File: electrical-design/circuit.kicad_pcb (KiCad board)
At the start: 4 copper layers, 100 x 70 mm, 42 parts, among them J1 AVR-ISP-10, J2 Conn_01x03_Female, J3 Conn_01x03_Female, Q1 2N3906, Q2 2N3906, Q3 2N3906, Q4 2N3906, SW1 SW_Push, SW2 SW_DIP_x04, SW3 SW_Push, U1 ATmega8A-P, U2 LTC-4627JD, U3 NE555P, Y1 16MHz

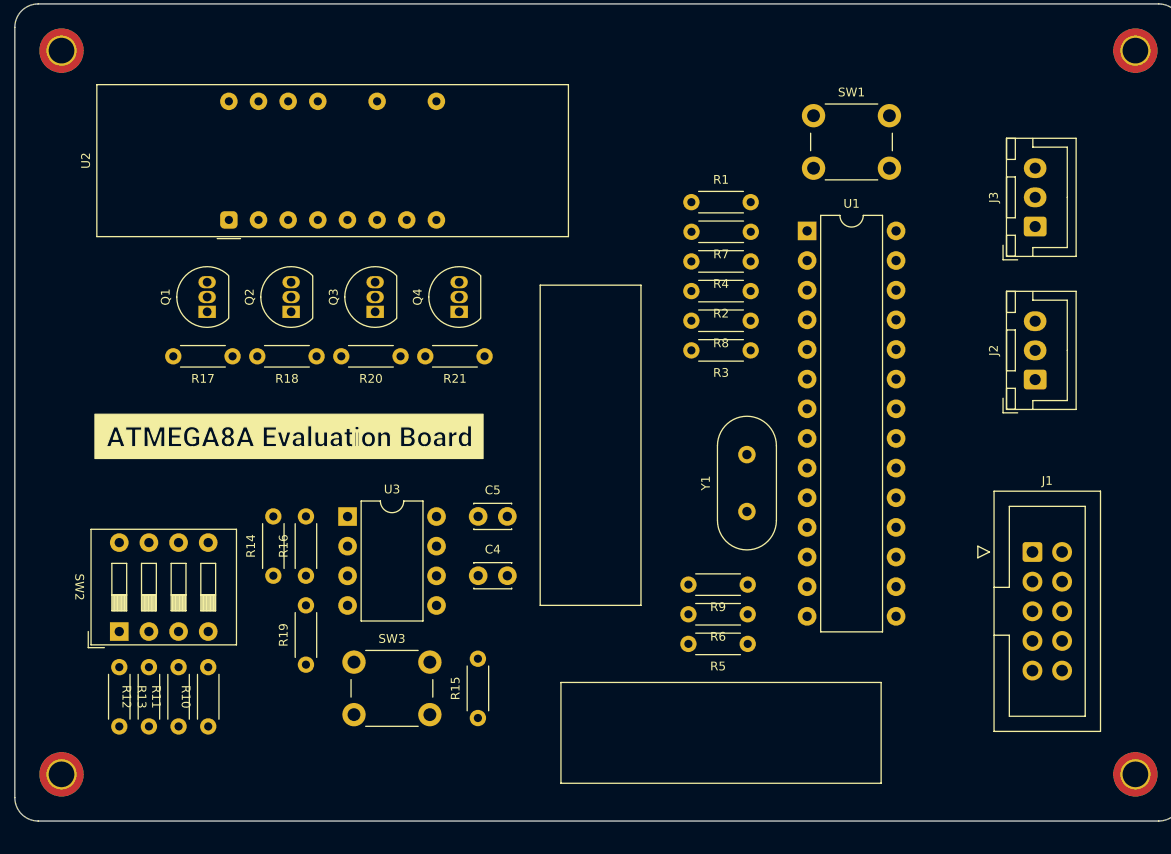
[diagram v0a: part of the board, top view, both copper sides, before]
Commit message: Added LED's to Board
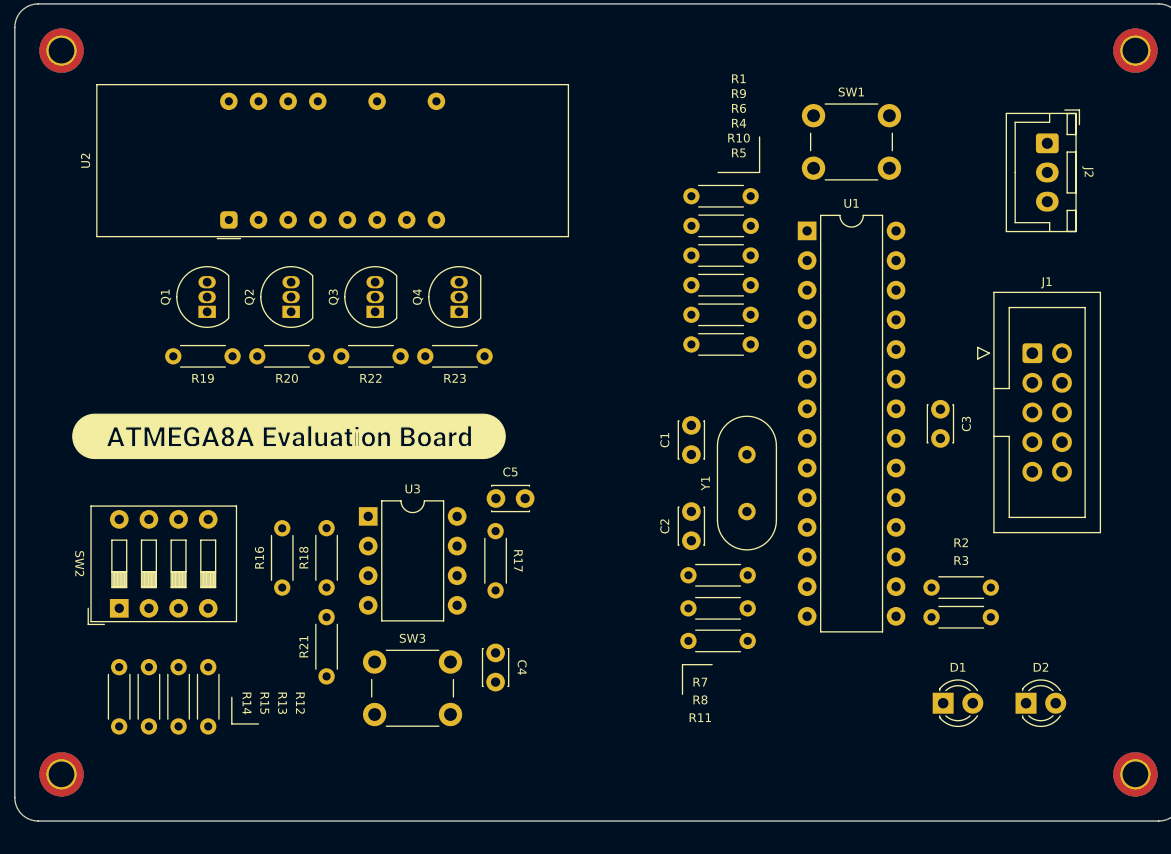
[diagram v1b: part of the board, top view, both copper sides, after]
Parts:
- removed J3: Conn_01x03_Female, Connector_JST:JST_XH_B3B-XH-A_1x03_P2.50mm_Vertical
- removed kibuzzard-63E112E7: G***, kibuzzard-63E112E7
- added C1: 22pF, Capacitor_THT:C_Disc_D3.0mm_W2.0mm_P2.50mm, F.Cu at (71.4, 52.1)
- added C2: 22pF, Capacitor_THT:C_Disc_D3.0mm_W2.0mm_P2.50mm, F.Cu at (71.4, 59.5)
- added C3: 0.1uF, Capacitor_THT:C_Disc_D3.0mm_W2.0mm_P2.50mm, F.Cu at (92.7, 48.2)
- added D1: LED, LED_THT:LED_D3.0mm, F.Cu at (92.9, 73.4)
- added D2: LED, LED_THT:LED_D3.0mm, F.Cu at (100.0, 73.4)
- added R2: 1K, Resistor_THT:R_Axial_DIN0204_L3.6mm_D1.6mm_P5.08mm_Horizontal, F.Cu at (91.9, 63.5)
- added R3: 1K, Resistor_THT:R_Axial_DIN0204_L3.6mm_D1.6mm_P5.08mm_Horizontal, F.Cu at (91.9, 66.0)
- added kibuzzard-63E126FF: G***, kibuzzard-63E126FF, F.Cu at (36.9, 50.5)
- moved J2 20.3 mm to (101.9, 25.4), turned to -90 degrees
- moved J1 17.0 mm to (100.6, 43.4)
- moved R17 16.1 mm to (54.6, 58.7), turned to -90 degrees
- moved C4 6.78 mm to (54.6, 69.1), turned to -90 degrees
- moved R7 5.88 mm to (76.2, 62.4)
- moved R15 5.08 mm to (22.4, 75.4), turned to 90 degrees
- moved R11 4.83 mm to (76.2, 68.1)
- moved C5 2.16 mm to (54.6, 55.9)
- moved R18 2.03 mm to (40.1, 63.5)
- moved R21 2.03 mm to (40.1, 71.1)
- moved SW2 1.99 mm to (22.4, 65.3)
- moved SW3 1.77 mm to (44.2, 69.9)
- moved U3 1.77 mm to (43.7, 57.4)
- moved R16 1.27 mm to (36.3, 63.5)
- moved R10 0.51 mm to (76.5, 40.1)
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- renumbered R8 to R10, R9 to R11, R10 to R12, R11 to R13, R12 to R14, R13 to R15, R14 to R16, R15 to R17, R16 to R18, R17 to R19, R18 to R20, R19 to R21, R20 to R22, R21 to R23, R2 to R4, R3 to R5, R4 to R6, R5 to R7, R6 to R8, R7 to R9
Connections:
- J2 pad 1: unconnected-(J2-Pad1) -> VCC
- J2 pad 2: unconnected-(J2-Pad2) -> Net-(U1-Pad27)
- J2 pad 3: unconnected-(J2-Pad3) -> GND
- R1 pad 2: Net-(U1-Pad1) -> ~{RESET}
- SW1 pad 2: Net-(U1-Pad1) -> ~{RESET}
- U1 pad 1: Net-(U1-Pad1) -> ~{RESET}
- U1 pad 11: DECIMAL -> D
- U1 pad 13: D -> DECIMAL
- U1 pad 15: unconnected-(U1-Pad15) -> Net-(U1-Pad15)
- U1 pad 16: unconnected-(U1-Pad16) -> Net-(U1-Pad16)
- U1 pad 27: unconnected-(U1-Pad27) -> Net-(U1-Pad27)
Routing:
- net Net-(R7-Pad2): track 0.00 -> 58.9 mm
- net ~{DIGIT_0}: track 0.00 -> 58.7 mm
- net Net-(R8-Pad2): track 0.00 -> 55.9 mm
- net Net-(R11-Pad2): track 0.00 -> 52.9 mm
- net ~{DIGIT_1}: track 0.00 -> 52.0 mm
- net Frequency: track 0.00 -> 46.0 mm
- net ~{DIGIT_2}: track 0.00 -> 45.4 mm
- net ~{DIGIT_3}: track 0.00 -> 39.7 mm
- net ~{RESET}: track 0.00 -> 38.4 mm
- net Net-(R16-Pad2): track 0.00 -> 35.6 mm
- net MOSI: track 0.00 -> 28.2 mm
- net Net-(C4-Pad1): track 0.00 -> 17.8 mm
- net SCK: track 0.00 -> 13.6 mm
- net MISO: track 0.00 -> 13.6 mm
- net Net-(C2-Pad2): track 0.00 -> 10.4 mm
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
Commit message: Completed Initial Design of Circuit Board
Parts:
- removed kibuzzard-63E126FF: G***, kibuzzard-63E126FF
- added kibuzzard-63E387B9: G***, kibuzzard-63E387B9, F.Cu at (81.3, 61.0)
- moved H4 126.0 mm to (143.0, 27.9)
- moved SW2 51.5 mm to (73.8, 68.6), turned to -90 degrees
- moved H3 49.6 mm to (61.0, 27.9)
- moved R2 46.7 mm to (133.3, 85.2), turned to 90 degrees
- moved C5 45.4 mm to (98.6, 67.1)
- moved U3 45.4 mm to (87.6, 68.6)
- moved R17 45.4 mm to (98.6, 69.8)
- moved SW3 45.4 mm to (88.2, 81.1)
- moved C4 45.0 mm to (98.6, 78.7)
- moved R15 44.9 mm to (66.1, 85.5)
- moved R12 44.9 mm to (73.8, 85.5)
- moved R14 44.9 mm to (68.7, 85.5)
- moved R13 44.9 mm to (71.2, 85.5)
- moved D1 44.9 mm to (136.3, 85.2)
- moved Q3 44.8 mm to (87.7, 51.0)
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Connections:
- net A renamed /A
- net B renamed /B
- net C renamed /C
- net D renamed /D
- net DECIMAL renamed /DEC
- net E renamed /E
- net F renamed /F
- net G renamed /G
- C3 pad 1: GND -> Net-(C3-Pad1)
- C3 pad 2: Net-(C3-Pad2) -> GND
- D1 pad 1: GND -> Net-(D1-Pad1)
- D1 pad 2: Net-(D1-Pad2) -> Net-(U1-Pad15)
- D2 pad 1: GND -> Net-(D2-Pad1)
- D2 pad 2: Net-(D2-Pad2) -> Net-(U1-Pad16)
- R12 pad 2: Net-(R12-Pad2) -> Net-(SW2-Pad8)
- R13 pad 2: Net-(R13-Pad2) -> Net-(SW2-Pad7)
- R14 pad 2: Net-(R14-Pad2) -> Net-(SW2-Pad6)
- R15 pad 2: Net-(R15-Pad2) -> Net-(SW2-Pad5)
- R18 pad 1: Frequency -> VCC
- R18 pad 2: VCC -> Frequency
- R2 pad 1: Net-(U1-Pad15) -> Net-(D1-Pad1)
- R2 pad 2: Net-(D1-Pad2) -> GND
- R3 pad 1: Net-(U1-Pad16) -> Net-(D2-Pad1)
- R3 pad 2: Net-(D2-Pad2) -> GND
- SW2 pad 1: Net-(R15-Pad2) -> Net-(R16-Pad2)
- SW2 pad 2: Net-(R14-Pad2) -> Net-(R16-Pad2)
- SW2 pad 3: Net-(R13-Pad2) -> Net-(R16-Pad2)
- SW2 pad 4: Net-(R12-Pad2) -> Net-(R16-Pad2)
- SW2 pad 5: Net-(R16-Pad2) -> Net-(SW2-Pad5)
- SW2 pad 6: Net-(R16-Pad2) -> Net-(SW2-Pad6)
- SW2 pad 7: Net-(R16-Pad2) -> Net-(SW2-Pad7)
- SW2 pad 8: Net-(R16-Pad2) -> Net-(SW2-Pad8)
- U1 pad 21: Net-(C3-Pad2) -> Net-(C3-Pad1)
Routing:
- net Net-(U1-Pad15): track 0.00 -> 17.8 mm
- net Net-(J2-Pad2): track 0.00 -> 16.7 mm
- net Net-(U1-Pad16): track 0.00 -> 15.3 mm
- net ~{DIGIT_3}: track 39.7 -> 31.1 mm, vias 0 -> 2
- net ~{RESET}: track 38.4 -> 45.2 mm
- net Net-(R4-Pad2): track 41.5 -> 35.2 mm
- net Net-(R6-Pad2): track 37.9 -> 31.6 mm
- net Net-(R9-Pad2): track 31.8 -> 25.5 mm
- net ~{DIGIT_2}: track 45.4 -> 39.6 mm, vias 0 -> 2
- net Net-(R21-Pad2): track 9.07 -> 14.9 mm
- net Net-(R15-Pad2): track 5.04 -> 0.00 mm
- net Net-(R14-Pad2): track 5.04 -> 0.00 mm
- net Net-(R13-Pad2): track 5.04 -> 0.00 mm
- net Net-(R12-Pad2): track 5.04 -> 0.00 mm
- net Net-(R10-Pad2): track 44.7 -> 40.0 mm
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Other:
- board size 100 x 70 mm -> 90 x 70 mm

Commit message: Commiting Missing Files
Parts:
- removed kibuzzard-63E387B9: G***, kibuzzard-63E387B9
- added kibuzzard-63E778F7: G***, kibuzzard-63E778F7, F.Cu at (81.3, 61.0)

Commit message: Added Production Files
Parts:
- moved R2 0.25 mm to (133.1, 85.2)
- moved R3 0.25 mm to (133.1, 76.8)

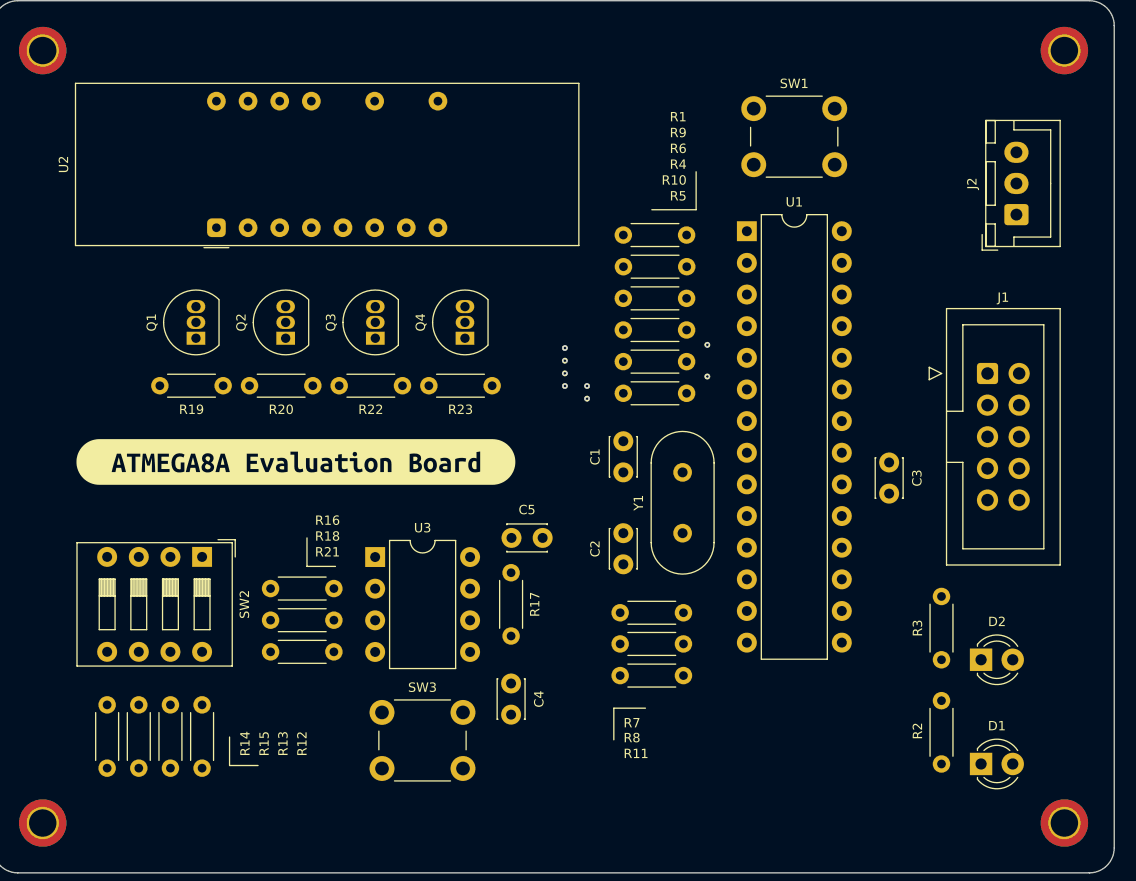
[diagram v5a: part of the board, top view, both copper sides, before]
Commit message: Approved Evaluation Board For Production
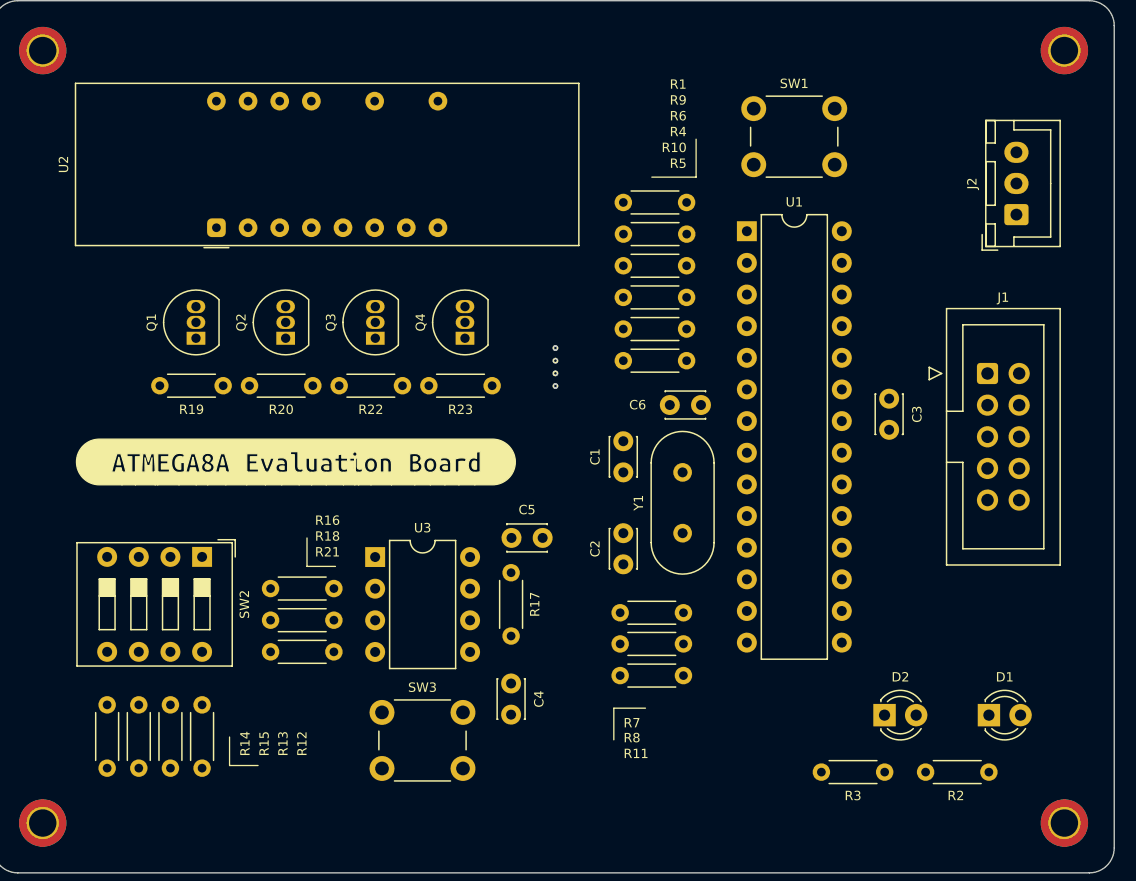
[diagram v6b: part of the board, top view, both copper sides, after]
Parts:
- added C6: 0.01uF, Capacitor_THT:C_Disc_D3.0mm_W2.0mm_P2.50mm, F.Cu at (113.8, 56.4)
- J2: value Conn_01x03_Female -> Analoge Header
- SW1, SW3: value SW_Push -> Reset Button
- moved R3 10.1 mm to (128.5, 85.9), turned to 180 degrees
- moved D2 8.93 mm to (128.5, 81.3)
- moved C3 5.12 mm to (128.9, 55.9)
- moved D1 3.97 mm to (136.9, 81.3)
- moved R2 3.86 mm to (136.9, 85.9), turned to 180 degrees
- moved R1 2.62 mm to (107.6, 40.1)
- moved R10 2.62 mm to (112.6, 50.3)
- moved R4 2.62 mm to (112.6, 47.8)
- moved R5 2.62 mm to (112.6, 52.8)
- moved R6 2.62 mm to (112.6, 45.2)
- moved R9 2.62 mm to (112.6, 42.7)
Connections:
- C3 pad 1: Net-(C3-Pad1) -> GND
- C3 pad 2: GND -> Net-(U1-AREF)
- D1 pad 2: Net-(D1-Pad2) -> Net-(D1-A)
- D2 pad 2: Net-(D2-Pad2) -> Net-(D2-A)
- U1 pad 15: Net-(D1-Pad2) -> Net-(D2-A)
- U1 pad 16: Net-(D2-Pad2) -> Net-(D1-A)
- U1 pad 21: Net-(C3-Pad1) -> Net-(U1-AREF)
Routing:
- net Net-(D1-A): track 0.00 -> 17.8 mm
- net Net-(D1-Pad2): track 17.8 -> 0.00 mm
- net Net-(D2-Pad2): track 15.3 -> 0.00 mm
- net Net-(D2-A): track 0.00 -> 9.27 mm
- net Net-(U1-AREF): track 0.00 -> 4.56 mm
- net Net-(C3-Pad1): track 4.12 -> 0.00 mm
- net Net-(U2-B): track 44.9 -> 42.2 mm
- net ~{DIGIT_1}: track 47.9 -> 45.5 mm, vias 2 -> 1
- net Net-(U2-G): track 40.0 -> 37.7 mm
- net ~{DIGIT_0}: track 55.0 -> 52.9 mm, vias 2 -> 1
- net ~{RESET}: track 45.2 -> 43.5 mm
- net Net-(D2-K): track 3.18 -> 4.58 mm
- net Net-(D1-K): track 3.18 -> 4.57 mm
- net Net-(U2-C): track 31.6 -> 30.5 mm
- net Net-(U2-F): track 25.5 -> 24.4 mm
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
